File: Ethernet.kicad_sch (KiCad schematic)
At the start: 30 parts, among them J1 7499111121A, U1 W5500, Y1 ECS-250-10-37B-CTN-TR

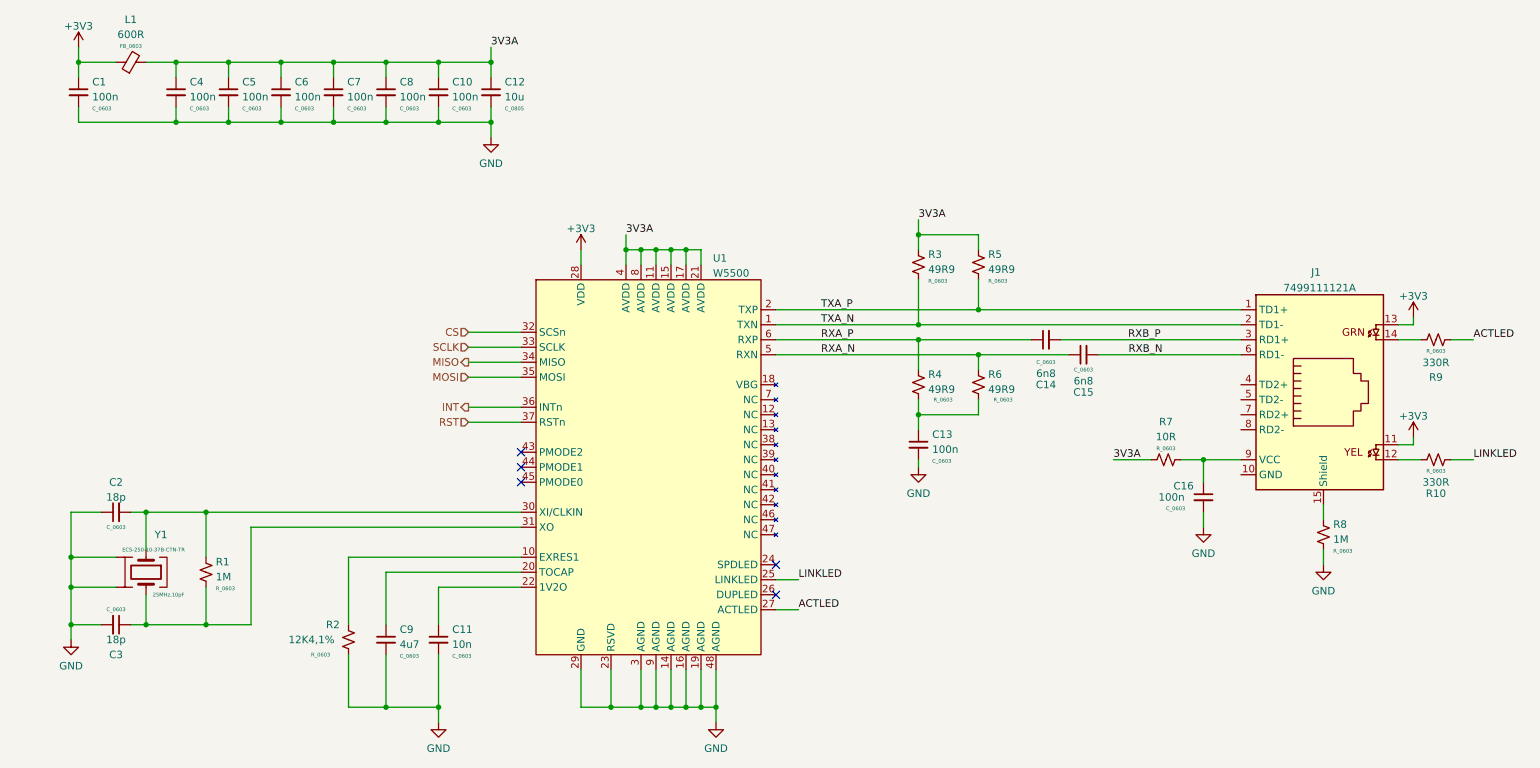
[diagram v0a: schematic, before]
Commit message: Rebuild using new output scripts
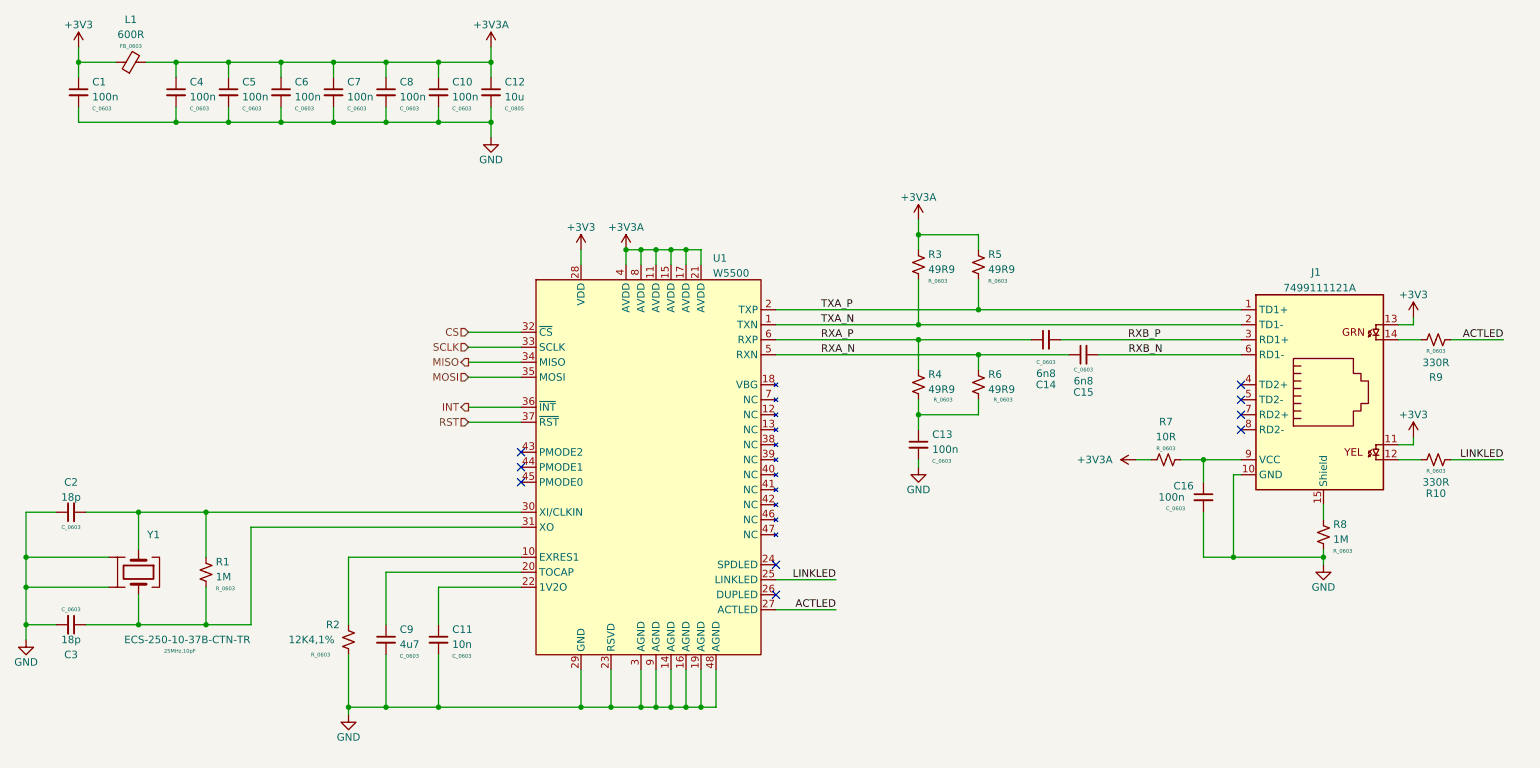
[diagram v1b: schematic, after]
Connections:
- net GND: now also J1.10 (GND)
- net 3V3A renamed +3V3A
- no-connect marks 5 -> 9
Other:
- company: (none) -> TL Embedded Ltd
- title: (none) -> Serial-Ethernet
- moved on the sheet: C2, C3, Y1
